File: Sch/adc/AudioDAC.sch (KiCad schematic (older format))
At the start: 22 parts, among them CN3 AudioJack, J7 JP2, U6 NAU8822LYG

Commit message: done except GND net
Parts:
- removed J7: JP2, adc_lib:M20-9980245, symbol JP2
- added C48, C49: 1uF, adc_lib:C0603, symbol C
- added L10, L7: L, adc_lib:FB0805, symbol L
- added R3: 10k, adc_lib:R0603, symbol R
- added U7: TLV702, adc_lib:TLV702, symbol TLV702
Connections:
- net labels added: VDDC
- net labels removed: VDD3
- wire segments 61 -> 74
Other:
- note added: "+3V"
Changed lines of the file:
@@
 $EndComp
 $Comp
-L GND #PWR052
+L GND #PWR053
 U 1 1 58A94BF7
 P 7300 4600
-F 0 "#PWR052" H 7300 4350 50  0001 C CNN
+F 0 "#PWR053" H 7300 4350 50  0001 C CNN
 F 1 "GND" H 7300 4450 50  0000 C CNN
 F 2 "" H 7300 4600 50  0000 C CNN
@@
 $EndComp
 $Comp
-L GND #PWR053
+L GND #PWR054
 U 1 1 58A96033
 P 5650 5100
-F 0 "#PWR053" H 5650 4850 50  0001 C CNN
+F 0 "#PWR054" H 5650 4850 50  0001 C CNN
 F 1 "GND" H 5650 4950 50  0000 C CNN
 F 2 "" H 5650 5100 50  0000 C CNN
@@
 $EndComp
 $Comp
-L +3V3 #PWR054
+L +3V3 #PWR055
 U 1 1 58A98414
 P 4750 1750
-F 0 "#PWR054" H 4750 1600 50  0001 C CNN
+F 0 "#PWR055" H 4750 1600 50  0001 C CNN
 F 1 "+3V3" H 4750 1890 50  0000 C CNN
 F 2 "" H 4750 1750 50  0000 C CNN
@@
 $EndComp
 $Comp
-L GND #PWR055
+L GND #PWR056
 U 1 1 58A98E4C
 P 7050 2800
-F 0 "#PWR055" H 7050 2550 50  0001 C CNN
+F 0 "#PWR056" H 7050 2550 50  0001 C CNN
 F 1 "GND" H 7050 2650 50  0000 C CNN
 F 2 "" H 7050 2800 50  0000 C CNN
@@
 $EndComp
 $Comp
-L GND #PWR056
+L GND #PWR057
 U 1 1 58A99758
 P 7700 2800
-F 0 "#PWR056" H 7700 2550 50  0001 C CNN
+F 0 "#PWR057" H 7700 2550 50  0001 C CNN
 F 1 "GND" H 7700 2650 50  0000 C CNN
 F 2 "" H 7700 2800 50  0000 C CNN
@@
 $EndComp
 $Comp
-L GND #PWR057
+L GND #PWR058
 U 1 1 58A997A8
 P 8300 2800
-F 0 "#PWR057" H 8300 2550 50  0001 C CNN
+F 0 "#PWR058" H 8300 2550 50  0001 C CNN
 F 1 "GND" H 8300 2650 50  0000 C CNN
 F 2 "" H 8300 2800 50  0000 C CNN
@@
 $EndComp
 $Comp
-L GND #PWR058
+L GND #PWR059
 U 1 1 58A99804
 P 8900 2800
-F 0 "#PWR058" H 8900 2550 50  0001 C CNN
+F 0 "#PWR059" H 8900 2550 50  0001 C CNN
 F 1 "GND" H 8900 2650 50  0000 C CNN
 F 2 "" H 8900 2800 50  0000 C CNN
@@
 	1    0    0    -1
 $EndComp
-Wire Wire Line
-	6250 3800 6450 3800
-Wire Wire Line
-	6450 3800 6450 3750
-Wire Wire Line
-	6450 3750 6750 3750
-Wire Wire Line
-	6250 3900 6450 3900
-Wire Wire Line
-	6450 3900 6450 4000
-Wire Wire Line
-	6450 4000 6750 4000
-Wire Wire Line
-	7050 4000 7600 4000
-Wire Wire Line
-	7600 4000 7600 3750
-Wire Wire Line
-	7600 3750 7850 3750
-Wire Wire Line
-	7450 3750 7450 3900
-Wire Wire Line
-	7450 3900 7850 3900
-Wire Wire Line
-	7500 4300 7500 3900
-Connection ~ 7500 3900
-Wire Wire Line
-	7300 4600 7950 4600
-Wire Wire Line
-	7850 3650 7700 3650
-Wire Wire Line
-	7700 3650 7700 4600
-Connection ~ 7500 4600
-Wire Wire Line
-	6250 3600 6600 3600
-Wire Wire Line
-	7950 4300 8300 4300
-Connection ~ 7700 4600
-Wire Wire Line
-	3700 4950 6500 4950
-Connection ~ 5400 4950
-Wire Wire Line
-	5650 4950 5650 5100
-Wire Wire Line
-	4650 4400 3900 4400
-Wire Wire Line
-	3900 4400 3900 4500
-Wire Wire Line
-	3900 4800 3900 4950
-Connection ~ 5300 4950
-Wire Wire Line
-	5050 1750 6750 1750
-Wire Wire Line
-	5500 1750 5500 2450
-Wire Wire Line
-	5600 1750 5600 2450
-Wire Wire Line
-	6800 2800 7050 2800
-Wire Wire Line
-	6800 2500 7050 2500
-Wire Wire Line
-	7450 2800 7700 2800
-Wire Wire Line
-	7450 2500 7700 2500
-Wire Wire Line
-	8050 2800 8300 2800
-Wire Wire Line
-	8050 2500 8300 2500
-Wire Wire Line
-	8650 2800 8900 2800
-Wire Wire Line
-	8650 2500 8900 2500
-Wire Wire Line
-	8650 1650 8650 2500
-Wire Wire Line
-	5600 2250 8050 2250
-Wire Wire Line
-	8050 2250 8050 2500
-Wire Wire Line
-	5500 2300 7450 2300
-Wire Wire Line
-	7450 2300 7450 2500
-Wire Wire Line
-	5400 2350 6800 2350
-Wire Wire Line
-	6800 2350 6800 2500
-Wire Wire Line
-	4650 4000 3700 4000
-Wire Wire Line
-	3700 4000 3700 4500
-Wire Wire Line
-	3700 4800 3700 4950
-Connection ~ 3900 4950
 NoConn ~ 6250 4200
 $Comp
@@
 	1    0    0    -1
 $EndComp
-Wire Wire Line
-	6250 4300 6500 4300
-Wire Wire Line
-	6500 4300 6500 4400
-Wire Wire Line
-	6500 4950 6500 4700
-Connection ~ 5650 4950
-Wire Wire Line
-	3050 4100 4650 4100
-Wire Wire Line
-	3050 4200 4650 4200
 $Comp
 L R R22
@@
 	1    0    0    -1
 $EndComp
+Text Notes 4750 2600 0    60   ~ 0
+100mW
+$Comp
+L TLV702 U7
+U 1 1 58B42AD2
+P 6800 1250
+F 0 "U7" H 6800 950 60  0000 C CNN
+F 1 "TLV702" H 6800 1550 60  0000 C CNN
+F 2 "adc_lib:TLV702" H 6800 950 60  0001 C CNN
+F 3 "" H 6800 950 60  0001 C CNN
+	1    6800 1250
+	1    0    0    -1
+$EndComp
+$Comp
+L +3V3 #PWR060
+U 1 1 58B42B1D
+P 5650 750
+F 0 "#PWR060" H 5650 600 50  0001 C CNN
+F 1 "+3V3" H 5650 890 50  0000 C CNN
+F 2 "" H 5650 750 50  0000 C CNN
+F 3 "" H 5650 750 50  0000 C CNN
+	1    5650 750
+	1    0    0    -1
+$EndComp
+$Comp
+L L L7
+U 1 1 58B42B5D
+P 5800 750
+F 0 "L7" V 5750 750 50  0000 C CNN
+F 1 "L" V 5875 750 50  0000 C CNN
+F 2 "adc_lib:FB0805" H 5800 750 50  0001 C CNN
+F 3 "" H 5800 750 50  0000 C CNN
+	1    5800 750
+	0    1    1    0
+$EndComp
+$Comp
+L C C48
+U 1 1 58B42C50
+P 5950 1250
+F 0 "C48" H 5975 1350 50  0000 L CNN
+F 1 "1uF" H 5975 1150 50  0000 L CNN
+F 2 "adc_lib:C0603" H 5988 1100 50  0001 C CNN
+F 3 "" H 5950 1250 50  0000 C CNN
+	1    5950 1250
+	1    0    0    -1
+$EndComp
+$Comp
+L R R3
+U 1 1 58B42CBF
+P 6250 1050
+F 0 "R3" V 6330 1050 50  0000 C CNN
+F 1 "10k" V 6250 1050 50  0000 C CNN
+F 2 "adc_lib:R0603" V 6180 1050 50  0001 C CNN
+F 3 "" H 6250 1050 50  0000 C CNN
+	1    6250 1050
+	1    0    0    -1
+$EndComp
+$Comp
+L GND #PWR061
+U 1 1 58B42E0C
+P 7250 1750
+F 0 "#PWR061" H 7250 1500 50  0001 C CNN
+F 1 "GND" H 7250 1600 50  0000 C CNN
+F 2 "" H 7250 1750 50  0000 C CNN
+F 3 "" H 7250 1750 50  0000 C CNN
+	1    7250 1750
+	1    0    0    -1
+$EndComp
+$Comp
+L C C49
+U 1 1 58B42FBD
+P 7600 1400
+F 0 "C49" H 7625 1500 50  0000 L CNN
+F 1 "1uF" H 7625 1300 50  0000 L CNN
+F 2 "adc_lib:C0603" H 7638 1250 50  0001 C CNN
+F 3 "" H 7600 1400 50  0000 C CNN
+	1    7600 1400
+	1    0    0    -1
+$EndComp
+$Comp
+L L L10
+U 1 1 58B43AAD
+P 7900 1150
+F 0 "L10" V 7850 1150 50  0000 C CNN
+F 1 "L" V 7975 1150 50  0000 C CNN
+F 2 "adc_lib:FB0805" H 7900 1150 50  0001 C CNN
+F 3 "" H 7900 1150 50  0000 C CNN
+	1    7900 1150
+	0    1    1    0
+$EndComp
+Wire Wire Line
+	6250 3800 6450 3800
+Wire Wire Line
+	6450 3800 6450 3750
+Wire Wire Line
+	6450 3750 6750 3750
+Wire Wire Line
+	6250 3900 6450 3900
+Wire Wire Line
+	6450 3900 6450 4000
+Wire Wire Line
+	6450 4000 6750 4000
+Wire Wire Line
+	7050 4000 7600 4000
+Wire Wire Line
+	7600 4000 7600 3750
+Wire Wire Line
+	7600 3750 7850 3750
+Wire Wire Line
+	7450 3750 7450 3900
+Wire Wire Line
+	7450 3900 7850 3900
+Wire Wire Line
+	7500 4300 7500 3900
+Connection ~ 7500 3900
+Wire Wire Line
+	7300 4600 7950 4600
+Wire Wire Line
+	7850 3650 7700 3650
+Wire Wire Line
+	7700 3650 7700 4600
+Connection ~ 7500 4600
+Wire Wire Line
+	6250 3600 6600 3600
+Wire Wire Line
+	7950 4300 8300 4300
+Connection ~ 7700 4600
+Wire Wire Line
+	3700 4950 6500 4950
+Connection ~ 5400 4950
+Wire Wire Line
+	5650 4950 5650 5100
+Wire Wire Line
+	4650 4400 3900 4400
+Wire Wire Line
+	3900 4400 3900 4500
+Wire Wire Line
+	3900 4800 3900 4950
+Connection ~ 5300 4950
+Wire Wire Line
+	5050 1750 5600 1750
+Wire Wire Line
+	5500 1750 5500 2450
+Wire Wire Line
+	5600 1750 5600 2450
+Wire Wire Line
+	6800 2800 7050 2800
+Wire Wire Line
+	6800 2500 7050 2500
+Wire Wire Line
+	7450 2800 7700 2800
+Wire Wire Line
+	7450 2500 7700 2500
+Wire Wire Line
+	8050 2800 8300 2800
+Wire Wire Line
+	8050 2500 8300 2500
+Wire Wire Line
+	8650 2800 8900 2800
+Wire Wire Line
+	8650 2500 8900 2500
+Wire Wire Line
+	8650 1150 8650 2500
+Wire Wire Line
+	5600 2250 8050 2250
+Wire Wire Line
+	8050 2250 8050 2500
+Wire Wire Line
+	5500 2300 7450 2300
+Wire Wire Line
+	7450 2300 7450 2500
+Wire Wire Line
+	5400 2350 6800 2350
+Wire Wire Line
+	6800 2350 6800 2500
+Wire Wire Line
+	4650 4000 3700 4000
+Wire Wire Line
+	3700 4000 3700 4500
+Wire Wire Line
+	3700 4800 3700 4950
+Connection ~ 3900 4950
+Wire Wire Line
+	6250 4300 6500 4300
+Wire Wire Line
+	6500 4300 6500 4400
+Wire Wire Line
+	6500 4950 6500 4700
+Connection ~ 5650 4950
+Wire Wire Line
+	3050 4100 4650 4100
+Wire Wire Line
+	3050 4200 4650 4200
 Wire Wire Line
 	4750 1750 3550 1750
@@
 	3350 3750 3350 4200
 Connection ~ 3350 4200
-Text GLabel 6750 1650 0    60   Input ~ 0
-VDD3
-$Comp
-L JP2 J7
-U 1 1 58A9B1E7
-P 7100 1650
-F 0 "J7" H 7100 1400 60  0000 C CNN
-F 1 "JP2" H 7100 1850 60  0000 C CNN
-F 2 "adc_lib:M20-9980245" H 7050 1750 60  0001 C CNN
-F 3 "" H 7050 1750 60  0001 C CNN
-	1    7100 1650
-	1    0    0    -1
-$EndComp
-Wire Wire Line
-	7450 1750 7450 1650
-Wire Wire Line
-	7450 1650 8650 1650
 Wire Wire Line
 	5700 2450 5700 2200
@@
 	5700 2200 8650 2200
 Connection ~ 8650 2200
-Text Notes 4750 2600 0    60   ~ 0
-100mW
 Wire Wire Line
 	5400 1750 5400 2450
-Connection ~ 5600 1750
 Connection ~ 5600 2250
 Connection ~ 5500 1750
@@
 	7050 3750 7450 3750
 Connection ~ 7300 4000
+Wire Wire Line
+	5950 750  6400 750
+Wire Wire Line
+	6250 1350 6400 1350
+Wire Wire Line
+	5950 1650 7600 1650
+Connection ~ 7250 1650
+Wire Wire Line
+	7250 1350 7250 1750
+Wire Wire Line
+	7250 1150 7750 1150
+Wire Wire Line
+	6400 1250 6350 1250
+Wire Wire Line
+	6350 1250 6350 1650
+Connection ~ 6350 1650
+Wire Wire Line
+	6400 750  6400 1150
+Connection ~ 6250 750
+Wire Wire Line
+	7600 1150 7600 1250
+Wire Wire Line
+	7600 1650 7600 1550
+Connection ~ 7600 1150
+Wire Wire Line
+	8050 1150 8650 1150
+Wire Wire Line
+	5950 1400 5950 1650
+Wire Wire Line
+	5950 1100 5950 750
+Wire Wire Line
+	6250 750  6250 900
+Wire Wire Line
+	6250 1350 6250 1200
+Text Label 8350 1150 0    60   ~ 0
+VDDC
+Text Notes 7300 1100 0    60   ~ 0
++3V
 $EndSCHEMATC

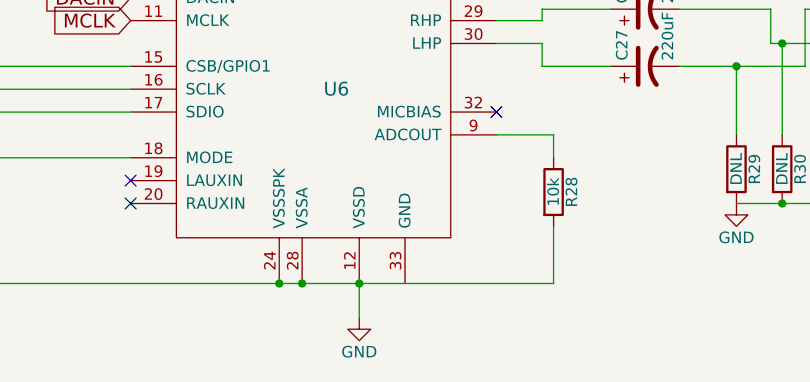
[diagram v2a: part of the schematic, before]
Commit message: Changed footprint for the Audio DAC. Silk arrangement
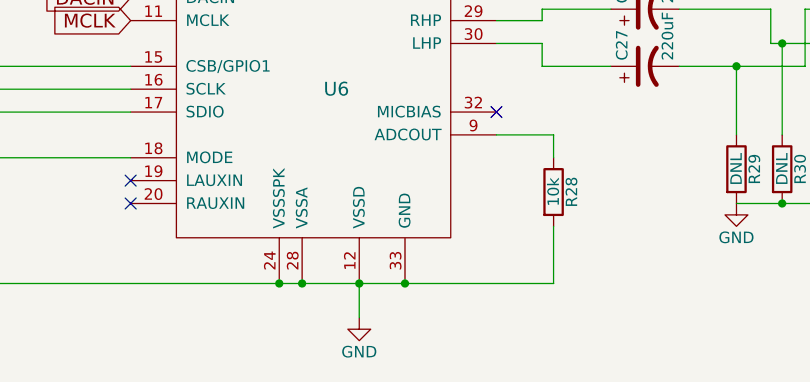
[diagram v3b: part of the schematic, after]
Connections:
- net GND: now also U6.33 (GND)
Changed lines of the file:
@@
 Text Notes 7300 1100 0    60   ~ 0
 +3V
+Connection ~ 5850 4950
 $EndSCHEMATC

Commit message: Changed some resistors to 0402.
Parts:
- R21, R22, R23: footprint adc_lib:R0603 -> adc_lib:R0402
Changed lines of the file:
@@
 F 0 "R23" V 3780 4650 50  0000 C CNN
 F 1 "10k" V 3700 4650 50  0000 C CNN
-F 2 "adc_lib:R0603" V 3630 4650 50  0001 C CNN
+F 2 "adc_lib:R0402" V 3630 4650 50  0001 C CNN
 F 3 "" H 3700 4650 50  0000 C CNN
 	1    3700 4650
@@
 F 0 "R22" V 3630 3600 50  0000 C CNN
 F 1 "10k" V 3550 3600 50  0000 C CNN
-F 2 "adc_lib:R0603" V 3480 3600 50  0001 C CNN
+F 2 "adc_lib:R0402" V 3480 3600 50  0001 C CNN
 F 3 "" H 3550 3600 50  0000 C CNN
 	1    3550 3600
@@
 F 0 "R21" V 3430 3600 50  0000 C CNN
 F 1 "10k" V 3350 3600 50  0000 C CNN
-F 2 "adc_lib:R0603" V 3280 3600 50  0001 C CNN
+F 2 "adc_lib:R0402" V 3280 3600 50  0001 C CNN
 F 3 "" H 3350 3600 50  0000 C CNN
 	1    3350 3600

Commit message: Changed PDS
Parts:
- removed L8: L, adc_lib:FB0805, symbol L
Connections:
- net +3V3: no longer R21.1, R22.1
- net at C28.1, C3.1, C41.1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: now also C48.1, L7.1, R21.1, R22.1, R3.1, U7.1 (IN)
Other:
- moved on the sheet: L7
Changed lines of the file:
@@
 	1    0    0    -1
-$EndComp
-$Comp
-L +3V3 #PWR055
-U 1 1 58A98414
-P 4750 1750
-F 0 "#PWR055" H 4750 1600 50  0001 C CNN
-F 1 "+3V3" H 4750 1890 50  0000 C CNN
-F 2 "" H 4750 1750 50  0000 C CNN
-F 3 "" H 4750 1750 50  0000 C CNN
-	1    4750 1750
-	1    0    0    -1
-$EndComp
-$Comp
-L L L8
-U 1 1 58A98450
-P 4900 1750
-F 0 "L8" V 4850 1750 50  0000 C CNN
-F 1 "L" V 4975 1750 50  0000 C CNN
-F 2 "adc_lib:FB0805" H 4900 1750 50  0001 C CNN
-F 3 "" H 4900 1750 50  0000 C CNN
-	1    4900 1750
-	0    1    1    0
 $EndComp
 Text GLabel 4650 3800 0    60   Input ~ 0
@@
 L +3V3 #PWR060
 U 1 1 58B42B1D
-P 5650 750
-F 0 "#PWR060" H 5650 600 50  0001 C CNN
-F 1 "+3V3" H 5650 890 50  0000 C CNN
-F 2 "" H 5650 750 50  0000 C CNN
-F 3 "" H 5650 750 50  0000 C CNN
-	1    5650 750
+P 4500 750
+F 0 "#PWR060" H 4500 600 50  0001 C CNN
+F 1 "+3V3" H 4500 890 50  0000 C CNN
+F 2 "" H 4500 750 50  0000 C CNN
+F 3 "" H 4500 750 50  0000 C CNN
+	1    4500 750
 	1    0    0    -1
 $EndComp
@@
 L L L7
 U 1 1 58B42B5D
-P 5800 750
-F 0 "L7" V 5750 750 50  0000 C CNN
-F 1 "L" V 5875 750 50  0000 C CNN
-F 2 "adc_lib:FB0805" H 5800 750 50  0001 C CNN
-F 3 "" H 5800 750 50  0000 C CNN
-	1    5800 750
+P 4650 750
+F 0 "L7" V 4600 750 50  0000 C CNN
+F 1 "L" V 4725 750 50  0000 C CNN
+F 2 "adc_lib:FB0805" H 4650 750 50  0001 C CNN
+F 3 "" H 4650 750 50  0000 C CNN
+	1    4650 750
 	0    1    1    0
 $EndComp
@@
 	0    1    1    0
 $EndComp
+Text Label 8350 1150 0    60   ~ 0
+VDDC
+Text Notes 7300 1100 0    60   ~ 0
++3V
 Wire Wire Line
 	6250 3800 6450 3800
@@
 Connection ~ 5300 4950
 Wire Wire Line
-	5050 1750 5600 1750
+	3550 1750 5600 1750
 Wire Wire Line
 	5500 1750 5500 2450
@@
 Wire Wire Line
 	3050 4200 4650 4200
-Wire Wire Line
-	4750 1750 3550 1750
 Wire Wire Line
 	3550 1750 3550 3450
@@
 Connection ~ 7300 4000
 Wire Wire Line
-	5950 750  6400 750
+	4800 750  6400 750
 Wire Wire Line
 	6250 1350 6400 1350
@@
 Wire Wire Line
 	6250 1350 6250 1200
-Text Label 8350 1150 0    60   ~ 0
-VDDC
-Text Notes 7300 1100 0    60   ~ 0
-+3V
 Connection ~ 5850 4950
+Connection ~ 5950 750
+Wire Wire Line
+	5050 1750 5050 750
+Connection ~ 5050 750
+Connection ~ 5050 1750
 $EndSCHEMATC
